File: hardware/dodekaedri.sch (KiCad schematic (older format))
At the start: 0 parts

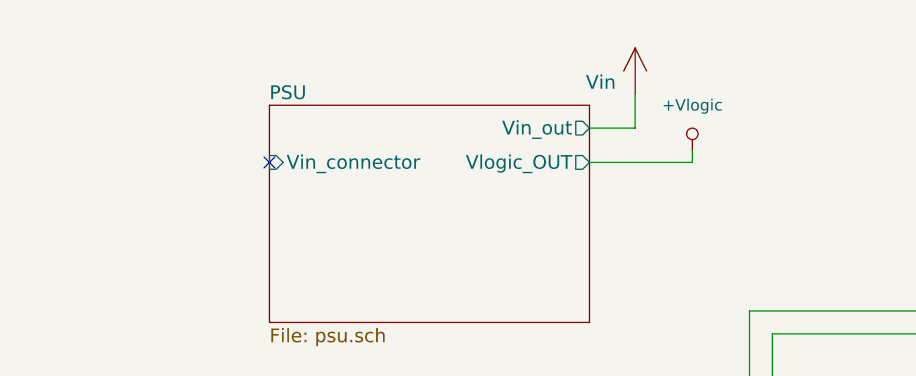
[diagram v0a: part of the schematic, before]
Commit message: fixed some ERC errors
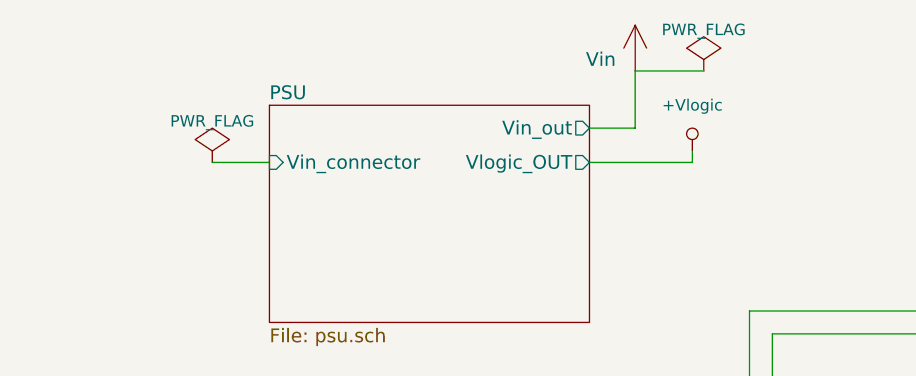
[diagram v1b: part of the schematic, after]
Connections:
- no-connect marks 1 -> 0
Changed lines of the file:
@@
 $EndSheet
 $Comp
-L +Vlogic #PWR101
+L +Vlogic #PWR01
 U 1 1 57E3367B
 P 5650 1900
-F 0 "#PWR101" H 5650 1700 50  0001 C CNN
+F 0 "#PWR01" H 5650 1700 50  0001 C CNN
 F 1 "+Vlogic" H 5650 2100 50  0000 C CNN
 F 2 "" H 5650 1900 50  0000 C CNN
@@
 Wire Wire Line
 	6000 4850 5300 4850
-NoConn ~ 3800 1950
-$Comp
-L Vin #Vin101
+$Comp
+L Vin #Vin02
 U 1 1 57E58C68
-P 5400 1650
-F 0 "#Vin101" H 5550 1700 60  0001 C CNN
-F 1 "Vin" H 5250 1700 60  0000 C CNN
-F 2 "" H 5400 1650 60  0001 C CNN
-F 3 "" H 5400 1650 60  0001 C CNN
-	1    5400 1650
+P 5400 1550
+F 0 "#Vin02" H 5550 1600 60  0001 C CNN
+F 1 "Vin" H 5250 1600 60  0000 C CNN
+F 2 "" H 5400 1550 60  0001 C CNN
+F 3 "" H 5400 1550 60  0001 C CNN
+	1    5400 1550
 	1    0    0    -1
 $EndComp
@@
 	5200 1800 5400 1800
 Wire Wire Line
-	5400 1800 5400 1650
+	5400 1800 5400 1550
 $Sheet
 S 3950 3000 1250 900
@@
 	1000 4000 1500 4000
 Connection ~ 9000 5100
+$Comp
+L PWR_FLAG #FLG?
+U 1 1 57EDEDF4
+P 5700 1550
+F 0 "#FLG?" H 5700 1645 50  0001 C CNN
+F 1 "PWR_FLAG" H 5700 1730 50  0000 C CNN
+F 2 "" H 5700 1550 50  0000 C CNN
+F 3 "" H 5700 1550 50  0000 C CNN
+	1    5700 1550
+	1    0    0    -1
+$EndComp
+Wire Wire Line
+	5400 1550 5700 1550
+$Comp
+L PWR_FLAG #FLG?
+U 1 1 57EDF2FE
+P 3550 1950
+F 0 "#FLG?" H 3550 2045 50  0001 C CNN
+F 1 "PWR_FLAG" H 3550 2130 50  0000 C CNN
+F 2 "" H 3550 1950 50  0000 C CNN
+F 3 "" H 3550 1950 50  0000 C CNN
+	1    3550 1950
+	1    0    0    -1
+$EndComp
+Wire Wire Line
+	3550 1950 3800 1950
 $EndSCHEMATC

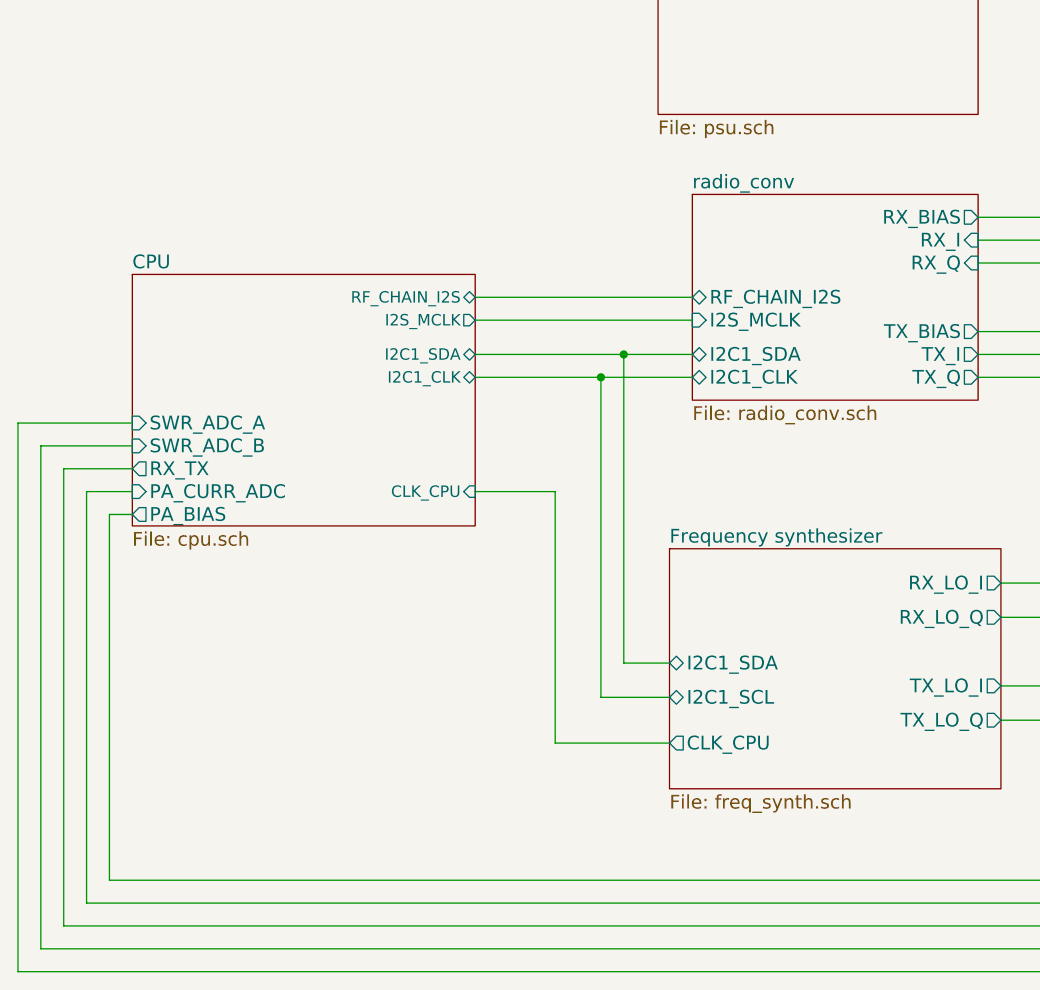
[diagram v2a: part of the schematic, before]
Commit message: Upgraded schematic to version 1.0 and generated initial BOM
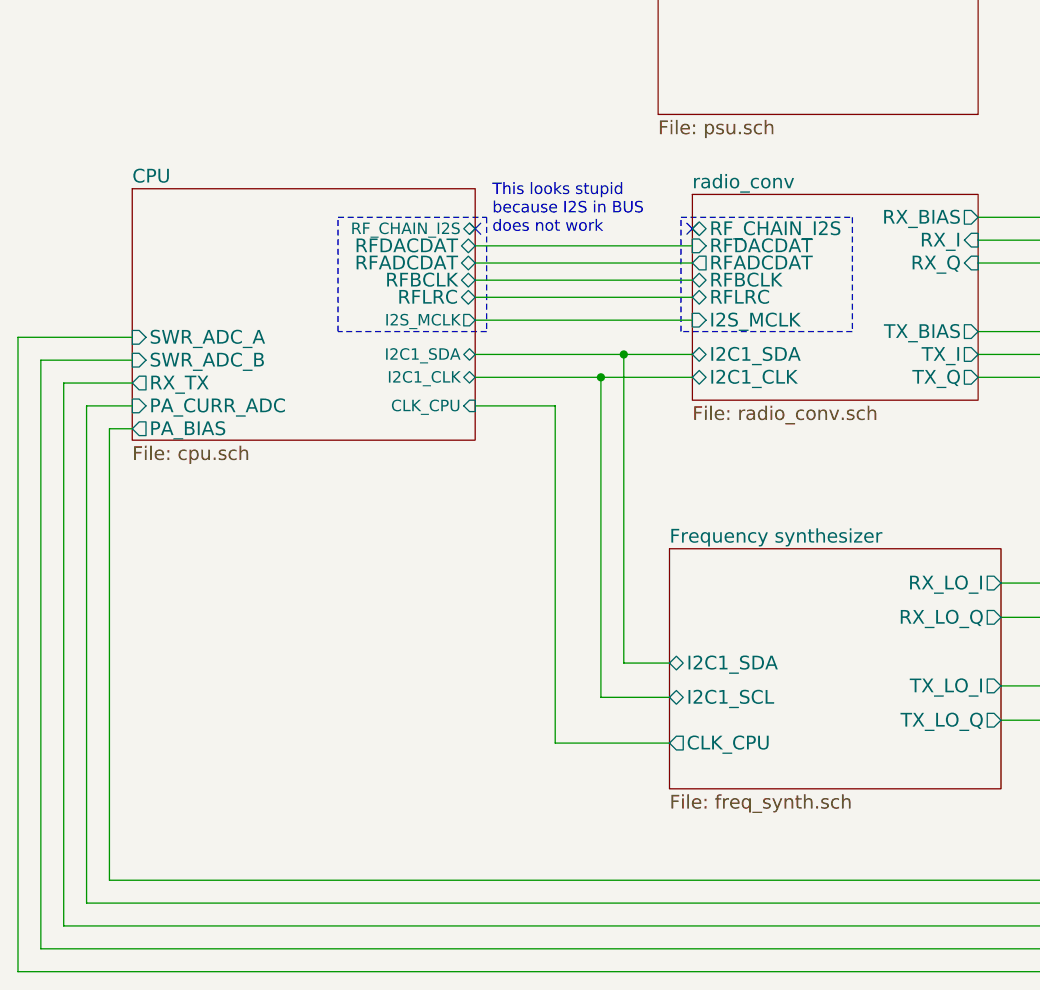
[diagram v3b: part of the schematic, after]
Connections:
- no-connect marks 0 -> 2
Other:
- note added: "This looks stupid\nbecause I2S in BUS\ndoes not work"
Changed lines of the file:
@@
 Sheet 1 8
 Title "Block layer"
-Date "2016-09-20"
-Rev "0.4"
+Date "2016-09-30"
+Rev "1.0"
 Comp "PRK - OH2TI"
 Comment1 "exla - OH2EHK"
@@
 $EndSheet
 $Comp
-L +Vlogic #PWR01
+L +Vlogic #PWR101
 U 1 1 57E3367B
 P 5650 1900
-F 0 "#PWR01" H 5650 1700 50  0001 C CNN
+F 0 "#PWR101" H 5650 1700 50  0001 C CNN
 F 1 "+Vlogic" H 5650 2100 50  0000 C CNN
 F 2 "" H 5650 1900 50  0000 C CNN
@@
 	6000 4850 5300 4850
 $Comp
-L Vin #Vin02
+L Vin #Vin101
 U 1 1 57E58C68
 P 5400 1550
-F 0 "#Vin02" H 5550 1600 60  0001 C CNN
+F 0 "#Vin101" H 5550 1600 60  0001 C CNN
 F 1 "Vin" H 5250 1600 60  0000 C CNN
 F 2 "" H 5400 1550 60  0001 C CNN
@@
 F0 "radio_conv" 60
 F1 "radio_conv.sch" 60
-F2 "RF_CHAIN_I2S" B L 3950 3450 60
+F2 "RF_CHAIN_I2S" B L 3950 3150 60
 F3 "I2C1_SDA" B L 3950 3700 60
 F4 "I2C1_CLK" B L 3950 3800 60
@@
 F10 "RX_BIAS" O R 5200 3100 60
 F11 "TX_BIAS" O R 5200 3600 60
+F12 "RFLRC" B L 3950 3450 60
+F13 "RFDACDAT" I L 3950 3225 60
+F14 "RFADCDAT" O L 3950 3300 60
+F15 "RFBCLK" B L 3950 3375 60
 $EndSheet
 Wire Wire Line
@@
 	6950 4750 7550 4750
 $Sheet
-S 1500 3350 1500 1100
+S 1500 2975 1500 1100
 U 57E5C816
 F0 "CPU" 60
@@
 F3 "I2C1_CLK" B R 3000 3800 50
 F4 "I2S_MCLK" O R 3000 3550 50
-F5 "RF_CHAIN_I2S" B R 3000 3450 50
-F6 "CLK_CPU" I R 3000 4300 50
-F7 "RX_TX" O L 1500 4200 60
-F8 "SWR_ADC_A" I L 1500 4000 60
-F9 "SWR_ADC_B" I L 1500 4100 60
-F10 "PA_CURR_ADC" I L 1500 4300 60
-F11 "PA_BIAS" O L 1500 4400 60
+F5 "RF_CHAIN_I2S" B R 3000 3150 50
+F6 "CLK_CPU" I R 3000 3925 50
+F7 "RX_TX" O L 1500 3825 60
+F8 "SWR_ADC_A" I L 1500 3625 60
+F9 "SWR_ADC_B" I L 1500 3725 60
+F10 "PA_CURR_ADC" I L 1500 3925 60
+F11 "PA_BIAS" O L 1500 4025 60
+F12 "RFDACDAT" B R 3000 3225 60
+F13 "RFADCDAT" B R 3000 3300 60
+F14 "RFBCLK" B R 3000 3375 60
+F15 "RFLRC" B R 3000 3450 60
 $EndSheet
 Connection ~ 3550 3800
@@
 	3000 3550 3950 3550
 Wire Wire Line
-	3000 3450 3950 3450
-Wire Wire Line
 	3850 5400 3350 5400
 Wire Wire Line
-	3350 5400 3350 4300
-Wire Wire Line
-	3350 4300 3000 4300
+	3350 5400 3350 3925
+Wire Wire Line
+	3350 3925 3000 3925
 Wire Wire Line
 	8650 5100 9300 5100
@@
 	9000 6200 1200 6200
 Wire Wire Line
-	1200 6200 1200 4200
-Wire Wire Line
-	1200 4200 1500 4200
+	1200 6200 1200 3825
+Wire Wire Line
+	1200 3825 1500 3825
 Wire Wire Line
 	8650 5200 8900 5200
@@
 	8900 6100 1300 6100
 Wire Wire Line
-	1300 6100 1300 4300
-Wire Wire Line
-	1300 4300 1500 4300
+	1300 6100 1300 3925
+Wire Wire Line
+	1300 3925 1500 3925
 Wire Wire Line
 	8650 5300 8800 5300
@@
 	8800 6000 1400 6000
 Wire Wire Line
-	1400 6000 1400 4400
-Wire Wire Line
-	1400 4400 1500 4400
+	1400 6000 1400 4025
+Wire Wire Line
+	1400 4025 1500 4025
 Wire Wire Line
 	9300 5200 9100 5200
@@
 	9100 6300 1100 6300
 Wire Wire Line
-	1100 6300 1100 4100
-Wire Wire Line
-	1100 4100 1500 4100
+	1100 6300 1100 3725
+Wire Wire Line
+	1100 3725 1500 3725
 Wire Wire Line
 	9300 5300 9200 5300
@@
 	9200 6400 1000 6400
 Wire Wire Line
-	1000 6400 1000 4000
-Wire Wire Line
-	1000 4000 1500 4000
+	1000 6400 1000 3625
+Wire Wire Line
+	1000 3625 1500 3625
 Connection ~ 9000 5100
 $Comp
-L PWR_FLAG #FLG03
+L PWR_FLAG #FLG102
 U 1 1 57EDEDF4
 P 5700 1550
-F 0 "#FLG03" H 5700 1645 50  0001 C CNN
+F 0 "#FLG102" H 5700 1645 50  0001 C CNN
 F 1 "PWR_FLAG" H 5700 1730 50  0000 C CNN
 F 2 "" H 5700 1550 50  0000 C CNN
@@
 	5400 1550 5700 1550
 $Comp
-L PWR_FLAG #FLG04
+L PWR_FLAG #FLG101
 U 1 1 57EDF2FE
 P 3550 1950
-F 0 "#FLG04" H 3550 2045 50  0001 C CNN
+F 0 "#FLG101" H 3550 2045 50  0001 C CNN
 F 1 "PWR_FLAG" H 3550 2130 50  0000 C CNN
 F 2 "" H 3550 1950 50  0000 C CNN
@@
 Wire Wire Line
 	3550 1950 3800 1950
+Wire Wire Line
+	3000 3225 3950 3225
+Wire Wire Line
+	3950 3300 3000 3300
+Wire Wire Line
+	3000 3375 3950 3375
+Wire Wire Line
+	3950 3450 3000 3450
+NoConn ~ 3000 3150
+NoConn ~ 3950 3150
+Wire Notes Line
+	2400 3100 3050 3100
+Wire Notes Line
+	3050 3100 3050 3600
+Wire Notes Line
+	3050 3600 2400 3600
+Wire Notes Line
+	2400 3600 2400 3100
+Wire Notes Line
+	3900 3100 4650 3100
+Wire Notes Line
+	4650 3100 4650 3600
+Wire Notes Line
+	4650 3600 3900 3600
+Wire Notes Line
+	3900 3600 3900 3100
+Text Notes 3075 3175 0    50   ~ 0
+This looks stupid\nbecause I2S in BUS\ndoes not work
 $EndSCHEMATC

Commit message: Fixed some bugs and annotated rest of the footprints
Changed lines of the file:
@@
 $EndSheet
 $Comp
-L +Vlogic #PWR101
+L +Vlogic #PWR01
 U 1 1 57E3367B
 P 5650 1900
-F 0 "#PWR101" H 5650 1700 50  0001 C CNN
+F 0 "#PWR01" H 5650 1700 50  0001 C CNN
 F 1 "+Vlogic" H 5650 2100 50  0000 C CNN
 F 2 "" H 5650 1900 50  0000 C CNN
@@
 	6000 4850 5300 4850
 $Comp
-L Vin #Vin101
+L Vin #Vin02
 U 1 1 57E58C68
 P 5400 1550
-F 0 "#Vin101" H 5550 1600 60  0001 C CNN
+F 0 "#Vin02" H 5550 1600 60  0001 C CNN
 F 1 "Vin" H 5250 1600 60  0000 C CNN
 F 2 "" H 5400 1550 60  0001 C CNN
@@
 Connection ~ 9000 5100
 $Comp
-L PWR_FLAG #FLG102
-U 1 1 57EDEDF4
-P 5700 1550
-F 0 "#FLG102" H 5700 1645 50  0001 C CNN
-F 1 "PWR_FLAG" H 5700 1730 50  0000 C CNN
-F 2 "" H 5700 1550 50  0000 C CNN
-F 3 "" H 5700 1550 50  0000 C CNN
-	1    5700 1550
-	1    0    0    -1
-$EndComp
-Wire Wire Line
-	5400 1550 5700 1550
-$Comp
-L PWR_FLAG #FLG101
+L PWR_FLAG #FLG03
 U 1 1 57EDF2FE
 P 3550 1950
-F 0 "#FLG101" H 3550 2045 50  0001 C CNN
+F 0 "#FLG03" H 3550 2045 50  0001 C CNN
 F 1 "PWR_FLAG" H 3550 2130 50  0000 C CNN
 F 2 "" H 3550 1950 50  0000 C CNN
